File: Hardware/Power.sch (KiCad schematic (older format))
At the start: 22 parts, among them P301 USB_B, P302 CONN_01X02, U301 MCP1700T, U302 FT232RQ

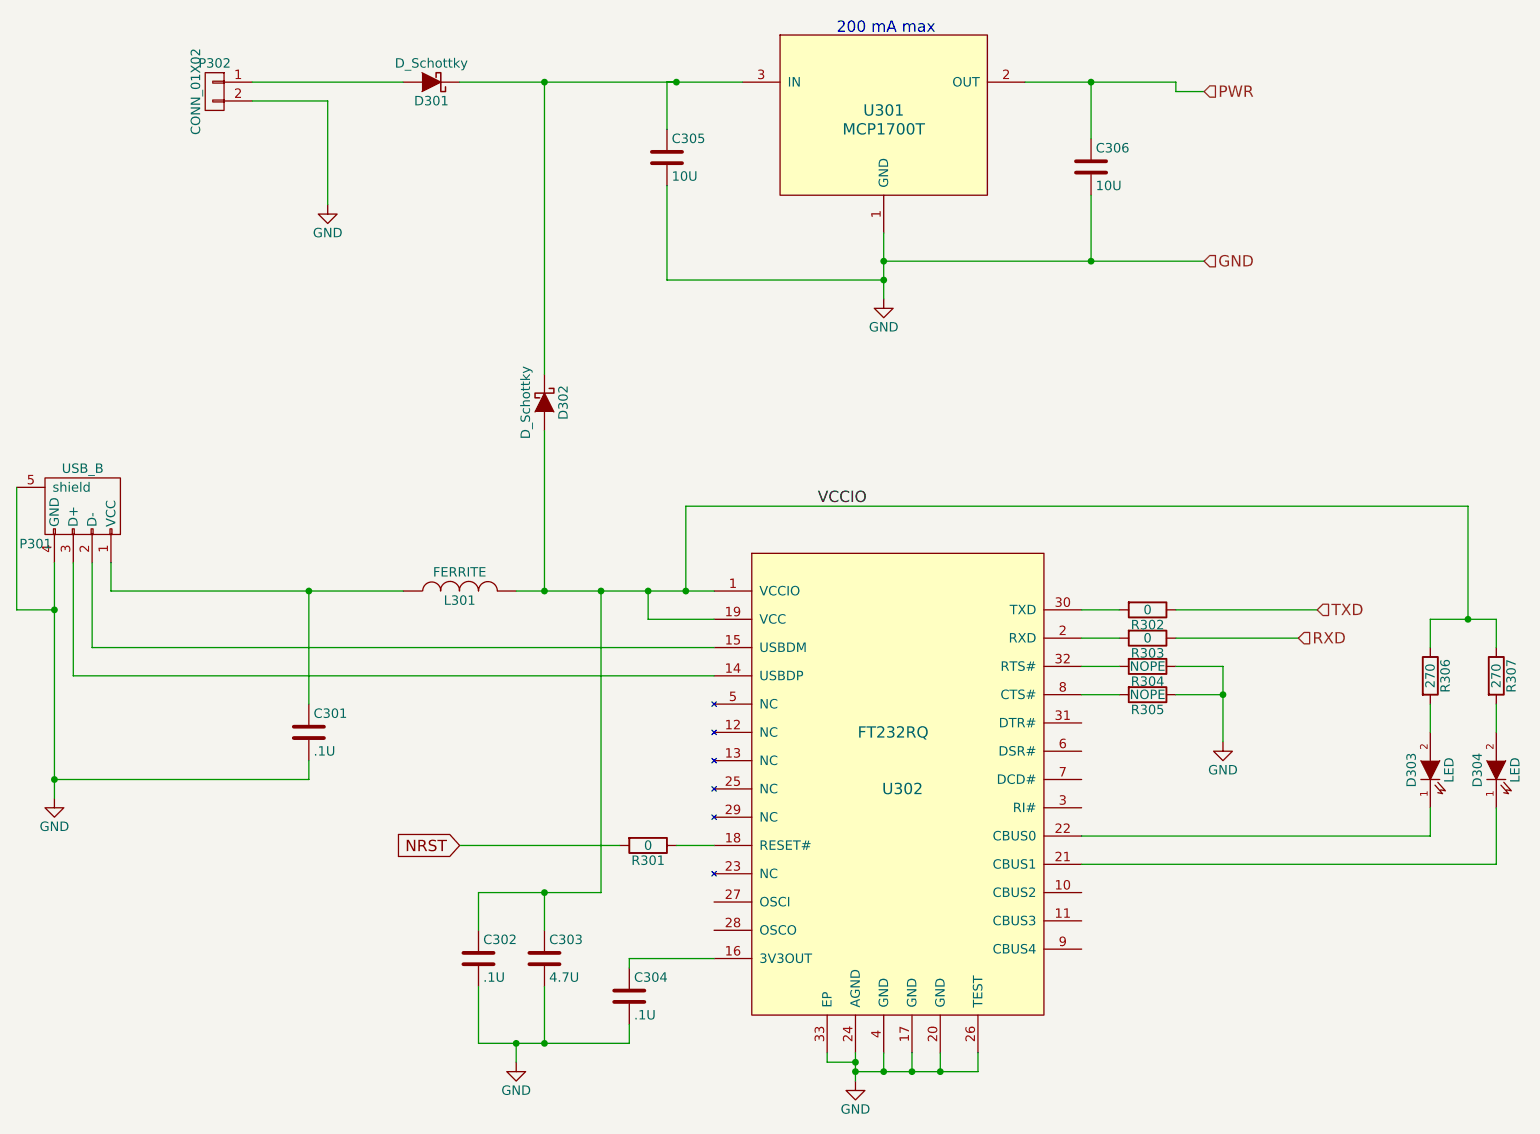
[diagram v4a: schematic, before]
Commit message: Changed the component values to hold MPNs for Macrofab processing
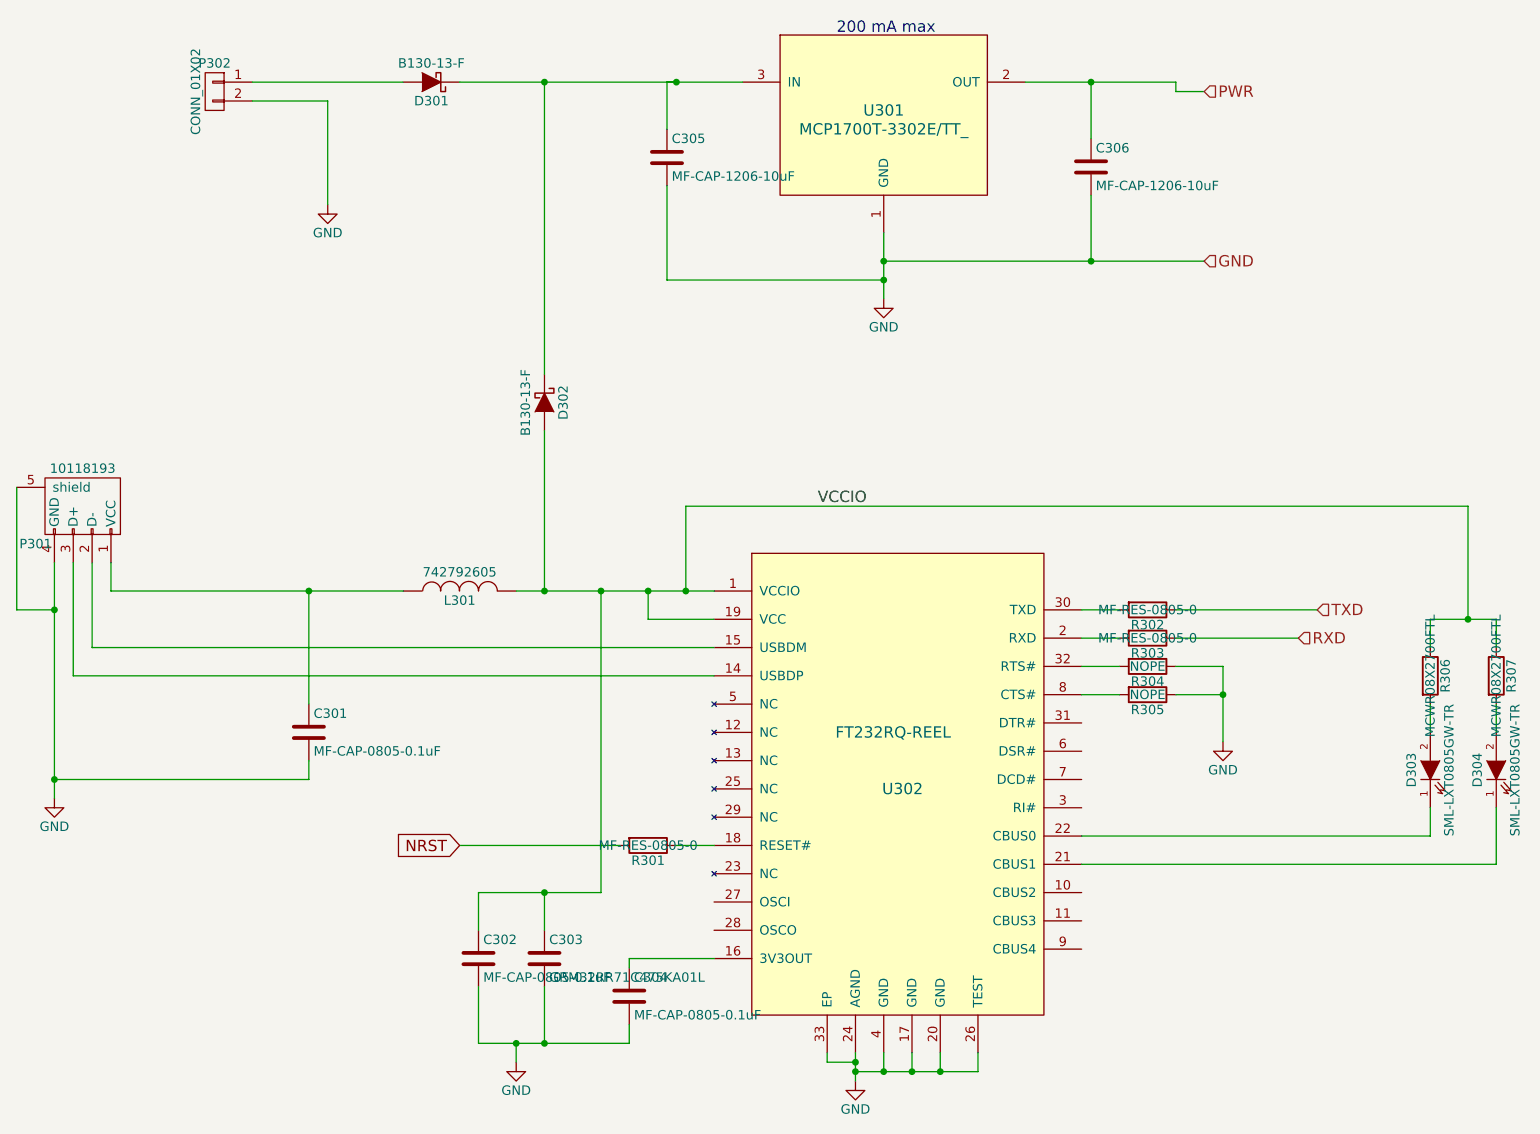
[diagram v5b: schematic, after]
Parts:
- C301, C302, C304: value .1U -> MF-CAP-0805-0.1uF
- C303: value 4.7U -> GRM32RR71C475KA01L
- C305: value 10U -> MF-CAP-1206-10uF
- C306: value 10U -> MF-CAP-1206-10uF; C1210C106Z4VACTU (none) -> C1210C106Z4VACTU; MPN C1210C106Z4VACTU -> (none)
- D301, D302: value D_Schottky -> B130-13-F
- D303, D304: value LED -> SML-LXT0805GW-TR
- L301: value FERRITE -> 742792605
- P301: value USB_B -> 10118193
- R301, R302, R303: value 0 -> MF-RES-0805-0
- R306, R307: value 270 -> MCWR08X2700FTL
- U301: value MCP1700T -> MCP1700T-3302E/TT_
- U302: value FT232RQ -> FT232RQ-REEL
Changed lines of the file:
@@
 P 5500 1100
 F 0 "U301" H 5500 1100 60  0000 C CNN
-F 1 "MCP1700T" H 5500 1000 60  0000 C CNN
+F 1 "MCP1700T-3302E/TT_" H 5500 1000 60  0000 C CNN
 F 2 "Housings_SOT-23_SOT-143_TSOT-6:SOT-23" H 5500 1100 60  0001 C CNN
 F 3 "" H 5500 1100 60  0000 C CNN
-F 4 "MCP1700T-3302E/TT_" H 5500 1100 60  0001 C CNN "MPN"
-F 5 "http://parts.io/detail/1370896/MCP1700T-3302E%2FTT" H 5500 1100 60  0001 C CNN "Link"
+F 4 "http://parts.io/detail/1370896/MCP1700T-3302E%2FTT" H 5500 1100 60  0001 C CNN "Link"
+F 5 "MCP1700T-3302E/TT_" H 5500 1100 60  0001 C CNN "MPN"
 F 6 "1296592" H 5500 1100 60  0001 C CNN "Farnell"
 	1    5500 1100
@@
 P 4350 1350
 F 0 "C305" H 4375 1450 50  0000 L CNN
-F 1 "10U" H 4375 1250 50  0000 L CNN
+F 1 "MF-CAP-1206-10uF" H 4375 1250 50  0000 L CNN
 F 2 "Capacitors_SMD:C_1210" H 4388 1200 30  0001 C CNN
 F 3 "" H 4350 1350 60  0000 C CNN
-F 4 "9227989" H 4350 1350 60  0001 C CNN "Farnell"
-F 5 "C1210C106Z4VACTU" H 4350 1350 60  0001 C CNN "MPN"
+F 4 "C1210C106Z4VACTU" H 4350 1350 60  0001 C CNN "MPN"
+F 5 "9227989" H 4350 1350 60  0001 C CNN "Farnell"
 	1    4350 1350
 	1    0    0    -1
@@
 P 6600 1400
 F 0 "C306" H 6625 1500 50  0000 L CNN
-F 1 "10U" H 6625 1300 50  0000 L CNN
+F 1 "MF-CAP-1206-10uF" H 6625 1300 50  0000 L CNN
 F 2 "Capacitors_SMD:C_1210" H 6638 1250 30  0001 C CNN
 F 3 "" H 6600 1400 60  0000 C CNN
-F 4 "9227989" H 6600 1400 60  0001 C CNN "Farnell"
-F 5 "C1210C106Z4VACTU" H 6600 1400 60  0001 C CNN "MPN"
+F 4 "C1210C106Z4VACTU" H 6600 1400 60  0001 C CNN "C1210C106Z4VACTU"
+F 5 "9227989" H 6600 1400 60  0001 C CNN "Farnell"
 	1    6600 1400
 	1    0    0    -1
@@
 P 5550 4750
 F 0 "U302" H 5600 4800 60  0000 C CNN
-F 1 "FT232RQ" H 5550 5100 60  0000 C CNN
+F 1 "FT232RQ-REEL" H 5550 5100 60  0000 C CNN
 F 2 "Housings_DFN_QFN:QFN-32-1EP_5x5mm_Pitch0.5mm" H 7700 4900 60  0001 C CNN
 F 3 "" H 7700 4900 60  0000 C CNN
-F 4 "FT232RQ-REEL" H 5550 4750 60  0001 C CNN "MPN"
-F 5 "http://parts.io/detail/3622205/FT232RQ-REEL" H 5550 4750 60  0001 C CNN "Link"
+F 4 "http://parts.io/detail/3622205/FT232RQ-REEL" H 5550 4750 60  0001 C CNN "Link"
+F 5 "FT232RQ-REEL" H 5550 4750 60  0001 C CNN "MPN"
 F 6 "1146033" H 5550 4750 60  0001 C CNN "Farnell"
 	1    5550 4750
@@
 P 1200 3200
 F 0 "P301" H 1400 3000 50  0000 C CNN
-F 1 "USB_B" H 1150 3400 50  0000 C CNN
+F 1 "10118193 " H 1150 3400 50  0000 C CNN
 F 2 "CentralCommand:10118193" V 1150 3100 60  0001 C CNN
 F 3 "" V 1150 3100 60  0000 C CNN
-F 4 "10118193 or USB3075-30-A" H 1200 3200 60  0001 C CNN "MPN"
-F 5 "http://parts.io/detail/93261255/10118193-0001LF" H 1200 3200 60  0001 C CNN "Link"
+F 4 "http://parts.io/detail/93261255/10118193-0001LF" H 1200 3200 60  0001 C CNN "Link"
+F 5 "10118193 or USB3075-30-A" H 1200 3200 60  0001 C CNN "MPN"
 F 6 "609-4616-1-ND" H 1200 3200 60  0001 C CNN "Digi-Key"
 F 7 "2443115" H 1200 3200 60  0001 C CNN "Farnell"
@@
 P 3250 3650
 F 0 "L301" V 3200 3650 50  0000 C CNN
-F 1 "FERRITE" V 3350 3650 50  0000 C CNN
+F 1 "742792605" V 3350 3650 50  0000 C CNN
 F 2 "Inductors_NEOSID:Neosid_Inductor_SM1206" H 3250 3650 60  0001 C CNN
 F 3 "" H 3250 3650 60  0000 C CNN
-F 4 "1800342" V 3250 3650 60  0001 C CNN "Farnell"
-F 5 "742792605" V 3250 3650 60  0001 C CNN "MPN"
+F 4 "742792605" V 3250 3650 60  0001 C CNN "MPN"
+F 5 "1800342" V 3250 3650 60  0001 C CNN "Farnell"
 	1    3250 3650
 	0    -1   -1   0
@@
 P 2450 4400
 F 0 "C301" H 2475 4500 50  0000 L CNN
-F 1 ".1U" H 2475 4300 50  0000 L CNN
+F 1 "MF-CAP-0805-0.1uF" H 2475 4300 50  0000 L CNN
 F 2 "Capacitors_SMD:C_0805" H 2488 4250 30  0001 C CNN
 F 3 "" H 2450 4400 60  0000 C CNN
@@
 P 3100 950
 F 0 "D301" H 3100 1050 50  0000 C CNN
-F 1 "D_Schottky" H 3100 850 50  0000 C CNN
+F 1 "B130-13-F" H 3100 850 50  0000 C CNN
 F 2 "Diodes_SMD:Diode-SMA_Standard" H 3100 950 60  0001 C CNN
 F 3 "" H 3100 950 60  0000 C CNN
-F 4 "B130-13-F" H 3100 950 60  0001 C CNN "MPN"
-F 5 "http://parts.io/detail/305034/B130-13-F" H 3100 950 60  0001 C CNN "Link"
+F 4 "http://parts.io/detail/305034/B130-13-F" H 3100 950 60  0001 C CNN "Link"
+F 5 "B130-13-F" H 3100 950 60  0001 C CNN "MPN"
 F 6 "1843713" H 3100 950 60  0001 C CNN "Farnell"
 	1    3100 950
@@
 P 3700 2650
 F 0 "D302" H 3700 2750 50  0000 C CNN
-F 1 "D_Schottky" H 3700 2550 50  0000 C CNN
+F 1 "B130-13-F" H 3700 2550 50  0000 C CNN
 F 2 "Diodes_SMD:Diode-SMA_Standard" H 3700 2650 60  0001 C CNN
 F 3 "" H 3700 2650 60  0000 C CNN
-F 4 "B130-13-F" H 3700 2650 60  0001 C CNN "MPN"
-F 5 "http://parts.io/detail/305034/B130-13-F" H 3700 2650 60  0001 C CNN "Link"
+F 4 "http://parts.io/detail/305034/B130-13-F" H 3700 2650 60  0001 C CNN "Link"
+F 5 "B130-13-F" H 3700 2650 60  0001 C CNN "MPN"
 F 6 "1843713" H 3700 2650 60  0001 C CNN "Farnell"
 	1    3700 2650
@@
 P 3700 5600
 F 0 "C303" H 3725 5700 50  0000 L CNN
-F 1 "4.7U" H 3725 5500 50  0000 L CNN
+F 1 "GRM32RR71C475KA01L" H 3725 5500 50  0000 L CNN
 F 2 "Capacitors_SMD:C_1210" H 3738 5450 30  0001 C CNN
 F 3 "" H 3700 5600 60  0000 C CNN
-F 4 "1845775" H 3700 5600 60  0001 C CNN "Farnell"
-F 5 "GRM32RR71C475KA01L" H 3700 5600 60  0001 C CNN "MPN"
+F 4 "GRM32RR71C475KA01L" H 3700 5600 60  0001 C CNN "MPN"
+F 5 "1845775" H 3700 5600 60  0001 C CNN "Farnell"
 	1    3700 5600
 	1    0    0    -1
@@
 P 3350 5600
 F 0 "C302" H 3375 5700 50  0000 L CNN
-F 1 ".1U" H 3375 5500 50  0000 L CNN
+F 1 "MF-CAP-0805-0.1uF" H 3375 5500 50  0000 L CNN
 F 2 "Capacitors_SMD:C_0805" H 3388 5450 30  0001 C CNN
 F 3 "" H 3350 5600 60  0000 C CNN
@@
 P 4150 5800
 F 0 "C304" H 4175 5900 50  0000 L CNN
-F 1 ".1U" H 4175 5700 50  0000 L CNN
+F 1 "MF-CAP-0805-0.1uF" H 4175 5700 50  0000 L CNN
 F 2 "Capacitors_SMD:C_0805" H 4188 5650 30  0001 C CNN
 F 3 "" H 4150 5800 60  0000 C CNN
-F 4 "2496944" H 4150 5800 60  0001 C CNN "Farnell"
-F 5 "0805B104K500CT" H 4150 5800 60  0001 C CNN "MPN"
+F 4 "0805B104K500CT" H 4150 5800 60  0001 C CNN "MPN"
+F 5 "2496944" H 4150 5800 60  0001 C CNN "Farnell"
 	1    4150 5800
 	1    0    0    -1
@@
 P 4250 5000
 F 0 "R301" V 4330 5000 50  0000 C CNN
-F 1 "0" V 4250 5000 50  0000 C CNN
+F 1 "MF-RES-0805-0" V 4250 5000 50  0000 C CNN
 F 2 "Resistors_SMD:R_0805" V 4180 5000 30  0001 C CNN
 F 3 "" H 4250 5000 30  0000 C CNN
@@
 P 8400 4100
 F 0 "R306" V 8480 4100 50  0000 C CNN
-F 1 "270" V 8400 4100 50  0000 C CNN
+F 1 "MCWR08X2700FTL" V 8400 4100 50  0000 C CNN
 F 2 "Resistors_SMD:R_0805" V 8330 4100 30  0001 C CNN
 F 3 "" H 8400 4100 30  0000 C CNN
-F 4 "2447618" V 8400 4100 60  0001 C CNN "Farnell"
-F 5 "MCWR08X2700FTL" V 8400 4100 60  0001 C CNN "MPN"
+F 4 "MCWR08X2700FTL" V 8400 4100 60  0001 C CNN "MPN"
+F 5 "2447618" V 8400 4100 60  0001 C CNN "Farnell"
 	1    8400 4100
 	1    0    0    -1
@@
 P 8400 4600
 F 0 "D303" H 8400 4700 50  0000 C CNN
-F 1 "LED" H 8400 4500 50  0000 C CNN
+F 1 "SML-LXT0805GW-TR" H 8400 4500 50  0000 C CNN
 F 2 "LEDs:LED-0805" H 8400 4600 60  0001 C CNN
 F 3 "" H 8400 4600 60  0000 C CNN
-F 4 "2062259" H 8400 4600 60  0001 C CNN "Farnell"
-F 5 "SML-LXT0805GW-TR" H 8400 4600 60  0001 C CNN "MPN"
+F 4 "SML-LXT0805GW-TR" H 8400 4600 60  0001 C CNN "MPN"
+F 5 "2062259" H 8400 4600 60  0001 C CNN "Farnell"
 	1    8400 4600
 	0    -1   -1   0
@@
 P 8750 4100
 F 0 "R307" V 8830 4100 50  0000 C CNN
-F 1 "270" V 8750 4100 50  0000 C CNN
+F 1 "MCWR08X2700FTL" V 8750 4100 50  0000 C CNN
 F 2 "Resistors_SMD:R_0805" V 8680 4100 30  0001 C CNN
 F 3 "" H 8750 4100 30  0000 C CNN
-F 4 "2447618" V 8750 4100 60  0001 C CNN "Farnell"
-F 5 "MCWR08X2700FTL" V 8750 4100 60  0001 C CNN "MPN"
+F 4 "MCWR08X2700FTL" V 8750 4100 60  0001 C CNN "MPN"
+F 5 "2447618" V 8750 4100 60  0001 C CNN "Farnell"
 	1    8750 4100
 	1    0    0    -1
@@
 P 8750 4600
 F 0 "D304" H 8750 4700 50  0000 C CNN
-F 1 "LED" H 8750 4500 50  0000 C CNN
+F 1 "SML-LXT0805GW-TR" H 8750 4500 50  0000 C CNN
 F 2 "LEDs:LED-0805" H 8750 4600 60  0001 C CNN
 F 3 "" H 8750 4600 60  0000 C CNN
-F 4 "2062259" H 8750 4600 60  0001 C CNN "Farnell"
-F 5 "SML-LXT0805GW-TR" H 8750 4600 60  0001 C CNN "MPN"
+F 4 "SML-LXT0805GW-TR" H 8750 4600 60  0001 C CNN "MPN"
+F 5 "2062259" H 8750 4600 60  0001 C CNN "Farnell"
 	1    8750 4600
 	0    -1   -1   0
@@
 P 6900 3750
 F 0 "R302" V 6980 3750 50  0000 C CNN
-F 1 "0" V 6900 3750 50  0000 C CNN
+F 1 "MF-RES-0805-0" V 6900 3750 50  0000 C CNN
 F 2 "Resistors_SMD:R_0805" V 6830 3750 30  0001 C CNN
 F 3 "" H 6900 3750 30  0000 C CNN
-F 4 "9333681" V 6900 3750 60  0001 C CNN "Farnell"
-F 5 "MC01W08050R" V 6900 3750 60  0001 C CNN "MPN"
+F 4 "MC01W08050R" V 6900 3750 60  0001 C CNN "MPN"
+F 5 "9333681" V 6900 3750 60  0001 C CNN "Farnell"
 	1    6900 3750
 	0    1    1    0
@@
 P 6900 3900
 F 0 "R303" V 6980 3900 50  0000 C CNN
-F 1 "0" V 6900 3900 50  0000 C CNN
+F 1 "MF-RES-0805-0" V 6900 3900 50  0000 C CNN
 F 2 "Resistors_SMD:R_0805" V 6830 3900 30  0001 C CNN
 F 3 "" H 6900 3900 30  0000 C CNN
